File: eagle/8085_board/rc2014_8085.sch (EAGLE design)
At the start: 17 parts, among them IC1 74HCT14N, IC3 74HCT573N

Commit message: Clean up, add CLK
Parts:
- R3, R4: value 10K -> 1K
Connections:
- net N$2 renamed ALE
- net N$3 renamed TX
- net N$4 renamed RX
- net CLK: now also IC2.CLK
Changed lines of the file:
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@@
 <?xml version="1.0" encoding="utf-8"?>
 <!DOCTYPE eagle SYSTEM "eagle.dtd">
-<eagle version="8.1.0">
+<eagle version="8.1.1">
 <drawing>
 <settings>
@@
 <part name="C2" library="rcl" deviceset="C-EU" device="050-024X044" value="0.1uF"/>
 <part name="R2" library="rcl" deviceset="R-US_" device="0207/10" value="10K"/>
-<part name="R3" library="rcl" deviceset="R-US_" device="0207/10" value="10K"/>
-<part name="R4" library="rcl" deviceset="R-US_" device="0207/10" value="10K"/>
+<part name="R3" library="rcl" deviceset="R-US_" device="0207/10" value="1K"/>
+<part name="R4" library="rcl" deviceset="R-US_" device="0207/10" value="1K"/>
 </parts>
 <sheets>
@@
 <pinref part="_PIN1" gate="-1" pin="14"/>
 <wire x1="-104.14" y1="149.86" x2="-35.56" y2="149.86" width="0.1524" layer="91"/>
-<wire x1="-35.56" y1="119.38" x2="-35.56" y2="149.86" width="0.1524" layer="91"/>
+<wire x1="-35.56" y1="116.84" x2="-35.56" y2="149.86" width="0.1524" layer="91"/>
 </segment>
 <segment>
@@
 <label x="-17.78" y="132.08" size="1.778" layer="95"/>
 </segment>
+<segment>
+<pinref part="IC2" gate="G$1" pin="CLK"/>
+<wire x1="17.78" y1="142.24" x2="15.24" y2="142.24" width="0.1524" layer="91"/>
+</segment>
 </net>
 <net name="/MREQ" class="0">
@@
 </segment>
 </net>
-<net name="N$2" class="0">
+<net name="ALE" class="0">
 <segment>
 <pinref part="IC3" gate="A" pin="C"/>
@@
 </segment>
 </net>
-<net name="N$3" class="0">
+<net name="TX" class="0">
 <segment>
 <pinref part="R4" gate="G$1" pin="1"/>
@@
 </segment>
 </net>
-<net name="N$4" class="0">
+<net name="RX" class="0">
 <segment>
 <pinref part="R3" gate="G$1" pin="1"/>
@@
 </sheet>
 </sheets>
+<errors>
+</errors>
 </schematic>
 </drawing>

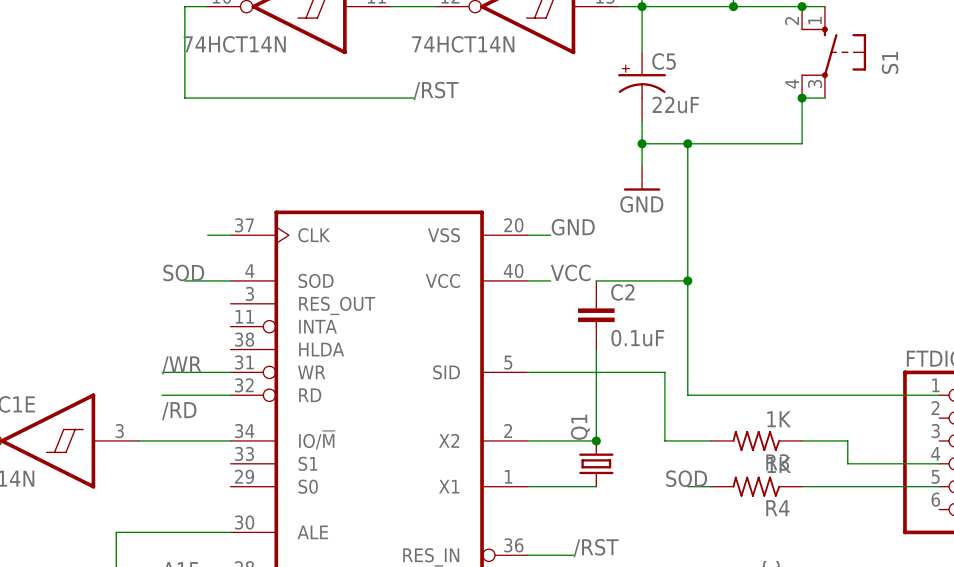
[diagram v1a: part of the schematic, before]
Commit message: Correct 20pF capacitor value for <4MHz crystal
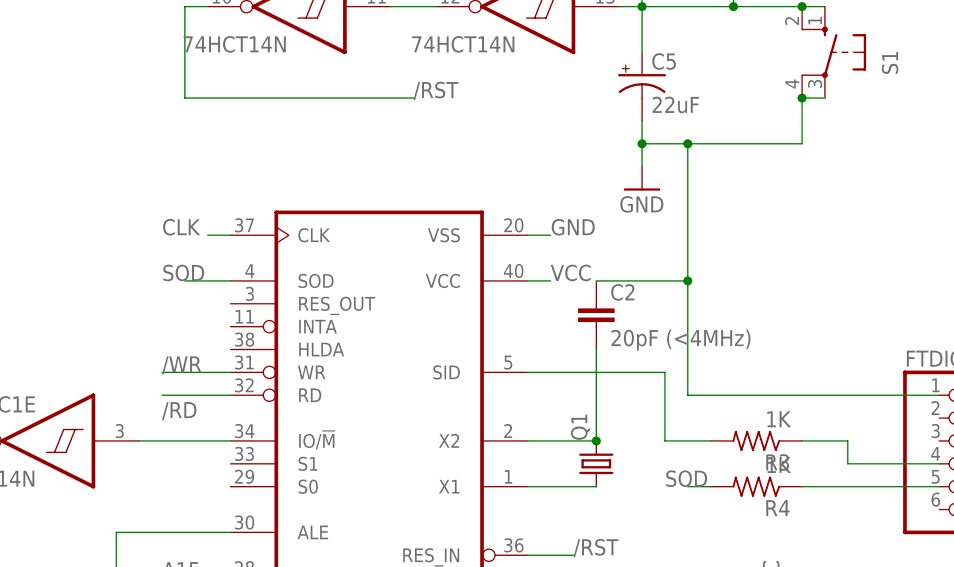
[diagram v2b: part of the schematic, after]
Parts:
- C2: value 0.1uF -> 20pF (<4MHz)
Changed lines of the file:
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@@
 <part name="Q1" library="crystal" deviceset="CRYSTAL" device="HC49S"/>
 <part name="FTDIGND" library="pinhead" deviceset="PINHD-1X6" device=""/>
-<part name="C2" library="rcl" deviceset="C-EU" device="050-024X044" value="0.1uF"/>
+<part name="C2" library="rcl" deviceset="C-EU" device="050-024X044" value="20pF (&lt;4MHz)"/>
 <part name="R2" library="rcl" deviceset="R-US_" device="0207/10" value="10K"/>
 <part name="R3" library="rcl" deviceset="R-US_" device="0207/10" value="1K"/>
@@
 <pinref part="IC2" gate="G$1" pin="CLK"/>
 <wire x1="17.78" y1="142.24" x2="15.24" y2="142.24" width="0.1524" layer="91"/>
-</segment>
-</net>
+<label x="10.16" y="142.24" size="1.778" layer="95"/>
+</segment>
+</net>
